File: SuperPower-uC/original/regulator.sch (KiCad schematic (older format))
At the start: 41 parts, among them Q701 DMP3028LSD, Q702 DMN3018SSD, Q703 2N7002A, U701 TPS63070RNMT, U702 TPS63070RNMT, U703 TPS70933DRVT

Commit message: Exchanged inductor of the regulators with IHLP2525CZER1R5M01
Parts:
- L701, L702: footprint Inductor_SMD:L_0603_1608Metric -> Inductor_SMD:L_Vishay_IHLP-2525; Ind_value (none) -> 1.5µH; Mfr_name (none) -> Vishay; Mfr_no (none) -> IHLP2525CZER1R5M01
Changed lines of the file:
@@
 F 0 "L701" V 6300 1750 50  0000 C CNN
 F 1 "1.5μH" V 6200 1750 50  0000 C CNN
-F 2 "Inductor_SMD:L_0603_1608Metric" H 6150 1750 50  0001 C CNN
-F 3 "https://datasheet.lcsc.com/szlcsc/TDK-MLZ1608A2R2WT000_C76797.pdf" H 6150 1750 50  0001 C CNN
+F 2 "Inductor_SMD:L_Vishay_IHLP-2525" H 6150 1750 50  0001 C CNN
+F 3 "https://www.mouser.de/datasheet/2/427/ihlp_2525cz_01-1763244.pdf" H 6150 1750 50  0001 C CNN
+F 4 "1.5µH" H 6150 1750 50  0001 C CNN "Ind_value"
+F 5 "Vishay" H 6150 1750 50  0001 C CNN "Mfr_name"
+F 6 "IHLP2525CZER1R5M01" H 6150 1750 50  0001 C CNN "Mfr_no"
 	1    6150 1750
 	0    -1   -1   0
@@
 F 0 "L702" V 6450 4800 50  0000 C CNN
 F 1 "1.5μH" V 6350 4800 50  0000 C CNN
-F 2 "Inductor_SMD:L_0603_1608Metric" H 6300 4800 50  0001 C CNN
-F 3 "https://datasheet.lcsc.com/szlcsc/TDK-MLZ1608A2R2WT000_C76797.pdf" H 6300 4800 50  0001 C CNN
+F 2 "Inductor_SMD:L_Vishay_IHLP-2525" H 6300 4800 50  0001 C CNN
+F 3 "https://www.mouser.de/datasheet/2/427/ihlp_2525cz_01-1763244.pdf" H 6300 4800 50  0001 C CNN
+F 4 "1.5µH" H 6300 4800 50  0001 C CNN "Ind_value"
+F 5 "Vishay" H 6300 4800 50  0001 C CNN "Mfr_name"
+F 6 "IHLP2525CZER1R5M01" H 6300 4800 50  0001 C CNN "Mfr_no"
 	1    6300 4800
 	0    -1   -1   0

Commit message: Changed regulator for 5V back to high side switching
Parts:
- removed R713: 100k, Resistor_SMD:R_0603_1608Metric, symbol Device:R_Small
- added JP3: Jumper_NC_Small, Connector_PinHeader_2.54mm:PinHeader_1x02_P2.54mm_Vertical, symbol Device:Jumper_NC_Small
- added Q9: 2N7002A, Package_TO_SOT_SMD:SOT-23, symbol 2n7002a:2N7002A
- added R18, R30: 1M, Resistor_SMD:R_0603_1608Metric, symbol Device:R_Small
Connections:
- net labels removed: GND_SW
- wire segments 184 -> 199
- no-connect marks 3 -> 1
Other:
- note added: "bypass\nEN_5V\n"
- moved on the sheet: C711, C712, C713, Q702A

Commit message: Update Buck-Boost inductors
Replace Vishay HILP series by TDK SPM series
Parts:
- removed L701, L702: 1.5μH, Inductor_SMD:L_Vishay_IHLP-2525, symbol Device:L
- added L701, L702: SPM6530T-1R5M, SPM6530T-1R5M:L_TDK_SPM6530T, symbol spm6530t-1r5m:SPM6530T-1R5M
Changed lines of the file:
@@
-$EndComp
-$Comp
-L Device:L L701
-U 1 1 5FBFC1E5
-P 6150 1750
-F 0 "L701" V 6300 1750 50  0000 C CNN
-F 1 "1.5μH" V 6200 1750 50  0000 C CNN
-F 2 "Inductor_SMD:L_Vishay_IHLP-2525" H 6150 1750 50  0001 C CNN
-F 3 "https://www.mouser.de/datasheet/2/427/ihlp_2525cz_01-1763244.pdf" H 6150 1750 50  0001 C CNN
-F 4 "1.5µH" H 6150 1750 50  0001 C CNN "Ind_value"
-F 5 "Vishay" H 6150 1750 50  0001 C CNN "Mfr_name"
-F 6 "IHLP2525CZER1R5M01" H 6150 1750 50  0001 C CNN "Mfr_no"
-	1    6150 1750
-	0    -1   -1   0
 $EndComp
 $Comp
@@
 	1    5400 5350
 	1    0    0    -1
-$EndComp
-$Comp
-L Device:L L702
-U 1 1 602F526D
-P 6300 4800
-F 0 "L702" V 6450 4800 50  0000 C CNN
-F 1 "1.5μH" V 6350 4800 50  0000 C CNN
-F 2 "Inductor_SMD:L_Vishay_IHLP-2525" H 6300 4800 50  0001 C CNN
-F 3 "https://www.mouser.de/datasheet/2/427/ihlp_2525cz_01-1763244.pdf" H 6300 4800 50  0001 C CNN
-F 4 "1.5µH" H 6300 4800 50  0001 C CNN "Ind_value"
-F 5 "Vishay" H 6300 4800 50  0001 C CNN "Mfr_name"
-F 6 "IHLP2525CZER1R5M01" H 6300 4800 50  0001 C CNN "Mfr_no"
-	1    6300 4800
-	0    -1   -1   0
 $EndComp
 Wire Wire Line
@@
 	8150 5850 8150 5600
 Connection ~ 8150 5600
+$Comp
+L spm6530t-1r5m:SPM6530T-1R5M L701
+U 1 1 5FDC75EF
+P 6150 1750
+F 0 "L701" V 6250 1850 50  0000 R CNN
+F 1 "SPM6530T-1R5M" V 6100 1900 50  0001 R CNN
+F 2 "SPM6530T-1R5M:L_TDK_SPM6530T" H 6150 1750 50  0001 C CNN
+F 3 "https://product.tdk.com/info/en/catalog/datasheets/inductor_commercial_power_spm6530_en.pdf" H 6150 1750 50  0001 C CNN
+F 4 "TDK" H 6150 1750 50  0001 C CNN "Mfr_name"
+F 5 "SPM6530T-1R5M100" H 6150 1750 50  0001 C CNN "Mfr_no"
+F 6 "6,5x7,1x3,0mm" H 6150 1750 50  0001 C CNN "Package"
+F 7 "1.5µH" V 6100 1850 50  0000 R CNN "Ind_value"
+F 8 "11.0A" H 6150 1750 50  0001 C CNN "Ind_current_max"
+F 9 "11.5A" H 6150 1750 50  0001 C CNN "Ind_current_sat_max"
+F 10 "9.70mOhm" V 6100 1850 50  0001 R CNN "Ind_DCR_typ"
+F 11 "20%" H 6150 1750 50  0001 C CNN "Ind_tol"
+F 12 ">10MHz" H 6150 1750 50  0001 C CNN "Ind_SFR"
+F 13 "https://octopart.com/spm6530t-1r5m100-tdk-9518783?r=sp" H 6150 1750 50  0001 C CNN "Octopart_link"
+F 14 "https://fr.farnell.com/tdk/spm6530t-1r5m100/inductance-1-5uh-20-blindee/dp/2215610?st=SPM6530T-1R5M100" H 6150 1750 50  0001 C CNN "Farnell_link"
+F 15 "2215610" H 6150 1750 50  0001 C CNN "Farnell_ref"
+F 16 "2020-12-16" H 6150 1750 50  0001 C CNN "Farnell_check_date"
+F 17 "1,36 €" H 6150 1750 50  0001 C CNN "Farnell_price_qt=1"
+F 18 "1,36 €" H 6150 1750 50  0001 C CNN "Farnell_price_qt=10"
+F 19 "0,738 €" H 6150 1750 50  0001 C CNN "Farnell_price_qt=100"
+F 20 "0,458 €" H 6150 1750 50  0001 C CNN "Farnell_price_qt=1000"
+F 21 "2" H 6150 1750 50  0001 C CNN "Farnell_stock"
+F 22 "https://lcsc.com/product-detail/Power-Inductors_TDK-SPM6530T-1R5M100_C76854.html" H 6150 1750 50  0001 C CNN "LCSC_link"
+F 23 "C76854" H 6150 1750 50  0001 C CNN "LCSC_ref"
+F 24 "2020-12-16" H 6150 1750 50  0001 C CNN "LCSC_check_date"
+F 25 "$0.1717" H 6150 1750 50  0001 C CNN "LCSC_price_qt=1"
+F 26 "$0.1324" H 6150 1750 50  0001 C CNN "LCSC_price_qt=10"
+F 27 "$0.1179" H 6150 1750 50  0001 C CNN "LCSC_price_qt=100"
+F 28 "$0.1131" H 6150 1750 50  0001 C CNN "LCSC_price_qt=1000"
+F 29 "10,496" H 6150 1750 50  0001 C CNN "LCSC_stock"
+F 30 "https://eu.mouser.com/ProductDetail/TDK/SPM6530T-1R5M100/?qs=chjFIDm9dbqQ8Uh0Ilzv2g%3D%3D" H 6150 1750 50  0001 C CNN "Mouser_link"
+F 31 "810-SPM6530T-1R5M100" H 6150 1750 50  0001 C CNN "Mouser_ref"
+F 32 "2020-12-16" H 6150 1750 50  0001 C CNN "Mouser_check_date"
+F 33 "$1.42" H 6150 1750 50  0001 C CNN "Mouser_price_qt=1"
+F 34 "$1.07" H 6150 1750 50  0001 C CNN "Mouser_price_qt=10"
+F 35 "$0.812" H 6150 1750 50  0001 C CNN "Mouser_price_qt=100"
+F 36 "$0.564" H 6150 1750 50  0001 C CNN "Mouser_price_qt=1000"
+F 37 "2,011" H 6150 1750 50  0001 C CNN "Mouser_stock"
+F 38 "-" H 6150 1750 50  0001 C CNN "RS_link"
+F 39 "-" H 6150 1750 50  0001 C CNN "RS_ref"
+F 40 "2020-12-16" H 6150 1750 50  0001 C CNN "RS_check_date"
+F 41 "-" H 6150 1750 50  0001 C CNN "RS_price_qt=1"
+F 42 "-" H 6150 1750 50  0001 C CNN "RS_price_qt=10"
+F 43 "-" H 6150 1750 50  0001 C CNN "RS_price_qt=100"
+F 44 "-" H 6150 1750 50  0001 C CNN "RS_price_qt=1000"
+F 45 "-" H 6150 1750 50  0001 C CNN "RS_stock"
+F 46 "TO_CHECK" H 6150 1750 50  0001 C CNN "Status"
+F 47 "1.00" H 6150 1750 50  0001 C CNN "Release_version"
+F 48 "2020-12-16" H 6150 1750 50  0001 C CNN "Release_date"
+F 49 "ManWithNoName" H 6150 1750 50  0001 C CNN "Designer"
+	1    6150 1750
+	0    -1   -1   0
+$EndComp
+$Comp
+L spm6530t-1r5m:SPM6530T-1R5M L702
+U 1 1 5FE1ED88
+P 6300 4800
+F 0 "L702" V 6400 4900 50  0000 R CNN
+F 1 "SPM6530T-1R5M" V 6250 4950 50  0001 R CNN
+F 2 "SPM6530T-1R5M:L_TDK_SPM6530T" H 6300 4800 50  0001 C CNN
+F 3 "https://product.tdk.com/info/en/catalog/datasheets/inductor_commercial_power_spm6530_en.pdf" H 6300 4800 50  0001 C CNN
+F 4 "TDK" H 6300 4800 50  0001 C CNN "Mfr_name"
+F 5 "SPM6530T-1R5M100" H 6300 4800 50  0001 C CNN "Mfr_no"
+F 6 "6,5x7,1x3,0mm" H 6300 4800 50  0001 C CNN "Package"
+F 7 "1.5µH" V 6250 4900 50  0000 R CNN "Ind_value"
+F 8 "11.0A" H 6300 4800 50  0001 C CNN "Ind_current_max"
+F 9 "11.5A" H 6300 4800 50  0001 C CNN "Ind_current_sat_max"
+F 10 "9.70mOhm" V 6250 4900 50  0001 R CNN "Ind_DCR_typ"
+F 11 "20%" H 6300 4800 50  0001 C CNN "Ind_tol"
+F 12 ">10MHz" H 6300 4800 50  0001 C CNN "Ind_SFR"
+F 13 "https://octopart.com/spm6530t-1r5m100-tdk-9518783?r=sp" H 6300 4800 50  0001 C CNN "Octopart_link"
+F 14 "https://fr.farnell.com/tdk/spm6530t-1r5m100/inductance-1-5uh-20-blindee/dp/2215610?st=SPM6530T-1R5M100" H 6300 4800 50  0001 C CNN "Farnell_link"
+F 15 "2215610" H 6300 4800 50  0001 C CNN "Farnell_ref"
+F 16 "2020-12-16" H 6300 4800 50  0001 C CNN "Farnell_check_date"
+F 17 "1,36 €" H 6300 4800 50  0001 C CNN "Farnell_price_qt=1"
+F 18 "1,36 €" H 6300 4800 50  0001 C CNN "Farnell_price_qt=10"
+F 19 "0,738 €" H 6300 4800 50  0001 C CNN "Farnell_price_qt=100"
+F 20 "0,458 €" H 6300 4800 50  0001 C CNN "Farnell_price_qt=1000"
+F 21 "2" H 6300 4800 50  0001 C CNN "Farnell_stock"
+F 22 "https://lcsc.com/product-detail/Power-Inductors_TDK-SPM6530T-1R5M100_C76854.html" H 6300 4800 50  0001 C CNN "LCSC_link"
+F 23 "C76854" H 6300 4800 50  0001 C CNN "LCSC_ref"
+F 24 "2020-12-16" H 6300 4800 50  0001 C CNN "LCSC_check_date"
+F 25 "$0.1717" H 6300 4800 50  0001 C CNN "LCSC_price_qt=1"
+F 26 "$0.1324" H 6300 4800 50  0001 C CNN "LCSC_price_qt=10"
+F 27 "$0.1179" H 6300 4800 50  0001 C CNN "LCSC_price_qt=100"
+F 28 "$0.1131" H 6300 4800 50  0001 C CNN "LCSC_price_qt=1000"
+F 29 "10,496" H 6300 4800 50  0001 C CNN "LCSC_stock"
+F 30 "https://eu.mouser.com/ProductDetail/TDK/SPM6530T-1R5M100/?qs=chjFIDm9dbqQ8Uh0Ilzv2g%3D%3D" H 6300 4800 50  0001 C CNN "Mouser_link"
+F 31 "810-SPM6530T-1R5M100" H 6300 4800 50  0001 C CNN "Mouser_ref"
+F 32 "2020-12-16" H 6300 4800 50  0001 C CNN "Mouser_check_date"
+F 33 "$1.42" H 6300 4800 50  0001 C CNN "Mouser_price_qt=1"
+F 34 "$1.07" H 6300 4800 50  0001 C CNN "Mouser_price_qt=10"
+F 35 "$0.812" H 6300 4800 50  0001 C CNN "Mouser_price_qt=100"
+F 36 "$0.564" H 6300 4800 50  0001 C CNN "Mouser_price_qt=1000"
+F 37 "2,011" H 6300 4800 50  0001 C CNN "Mouser_stock"
+F 38 "-" H 6300 4800 50  0001 C CNN "RS_link"
+F 39 "-" H 6300 4800 50  0001 C CNN "RS_ref"
+F 40 "2020-12-16" H 6300 4800 50  0001 C CNN "RS_check_date"
+F 41 "-" H 6300 4800 50  0001 C CNN "RS_price_qt=1"
+F 42 "-" H 6300 4800 50  0001 C CNN "RS_price_qt=10"
+F 43 "-" H 6300 4800 50  0001 C CNN "RS_price_qt=100"
+F 44 "-" H 6300 4800 50  0001 C CNN "RS_price_qt=1000"
+F 45 "-" H 6300 4800 50  0001 C CNN "RS_stock"
+F 46 "TO_CHECK" H 6300 4800 50  0001 C CNN "Status"
+F 47 "1.00" H 6300 4800 50  0001 C CNN "Release_version"
+F 48 "2020-12-16" H 6300 4800 50  0001 C CNN "Release_date"
+F 49 "ManWithNoName" H 6300 4800 50  0001 C CNN "Designer"
+	1    6300 4800
+	0    -1   -1   0
+$EndComp
 $EndSCHEMATC

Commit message: Re-Annotate project
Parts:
- renumbered C710 to C14, C709 to C15, C701 to C16, C702 to C17, C711 to C18, C703 to C19, C712 to C20, C713 to C21, C707 to C22, C717 to C23, C708 to C24, C718 to C25, C704 to C26, C714 to C27, C705 to C28, C715 to C29, C706 to C30, C716 to C31, L701 to L2, L702 to L3, Q703 to Q10, Q9 to Q11, Q701 to Q5, Q702 to Q9, R711 to R39, R17 to R40, R18 to R41, R16 to R42, R30 to R43, R705 to R44, R709 to R45, R704 to R46, R703 to R47, R708 to R48, R707 to R49, R701 to R50, R706 to R51, TP37 to TP32, TP41 to TP33, U702 to U10, U703 to U8, U701 to U9
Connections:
- net EN_3V3: now also Q9.2 (G); no longer Q9.4 (G)
- net GND: now also Q9.1 (S); no longer Q9.3 (S)
- net GND_3v3: now also Q9.7 (D), Q9.8 (D); no longer Q9.5 (D), Q9.6 (D)
- net VIN: now also Q9.5 (D), Q9.6 (D); no longer Q9.7 (D), Q9.8 (D)
- net at JP3.1, Q11.3 (D), R43.1: now also Q9.4 (G); no longer Q9.2 (G)
- net at C18.1, C20.1, C21.1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: now also Q9.3 (S); no longer Q9.1 (S)

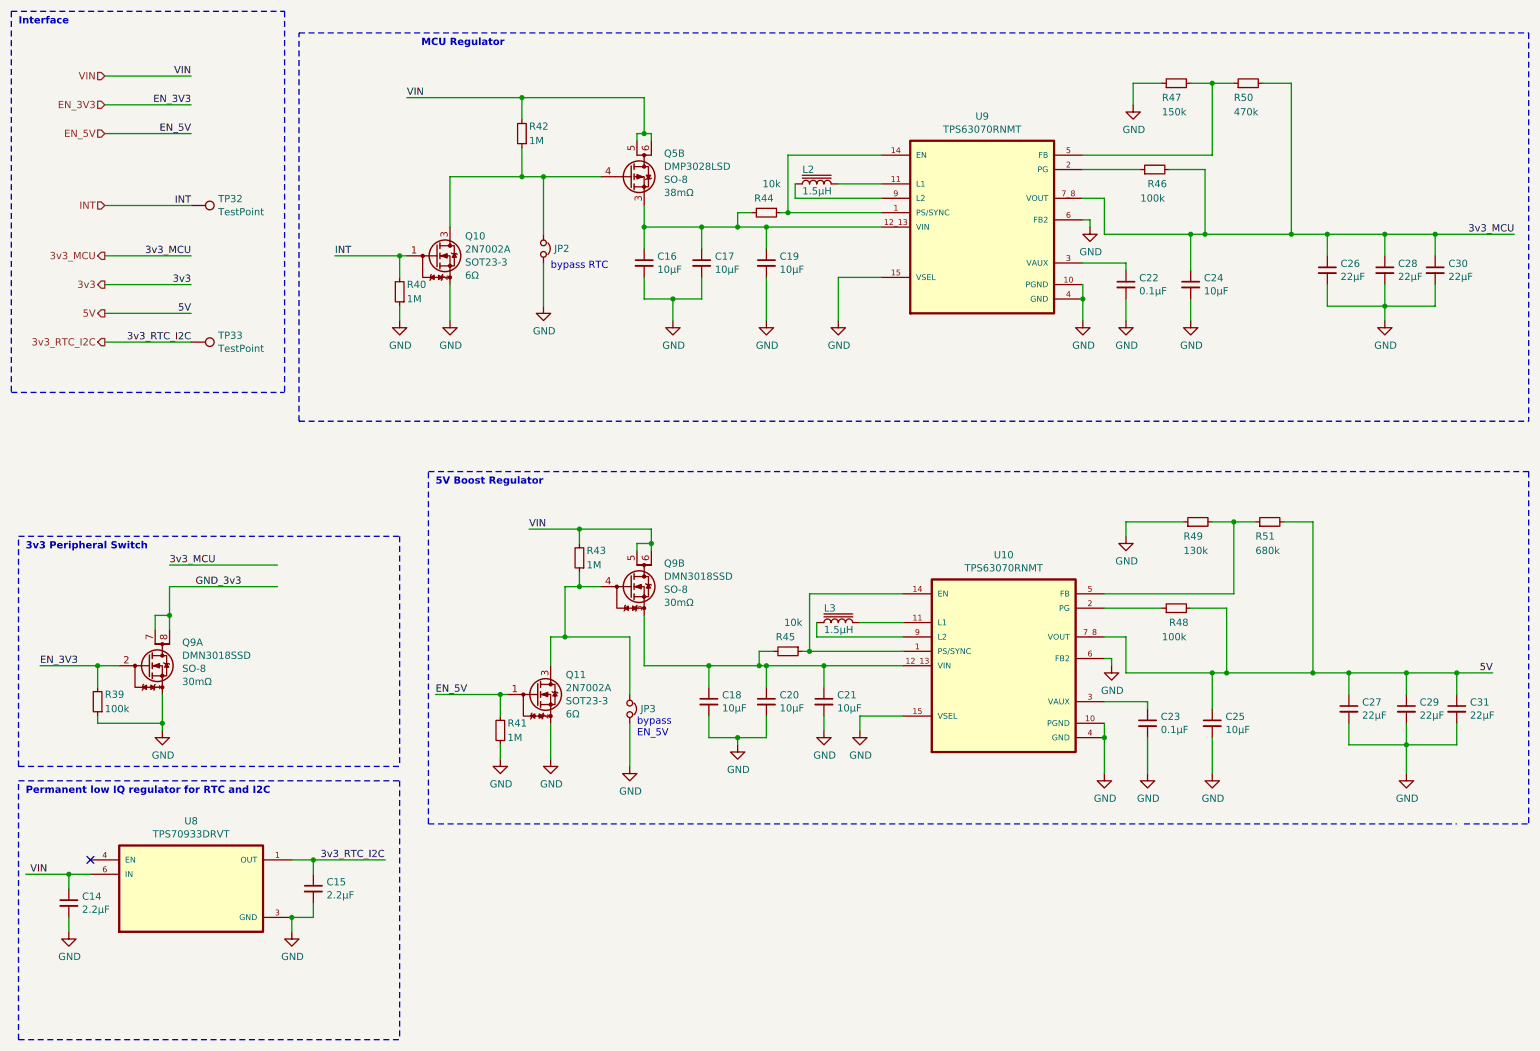
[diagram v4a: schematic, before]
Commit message: Replace some dual P-MOSFETs by SOT23-6 P-MOSFETs
+ resolve some issues (2 P-MOSFETs at Buck-Boost stage were reversed)
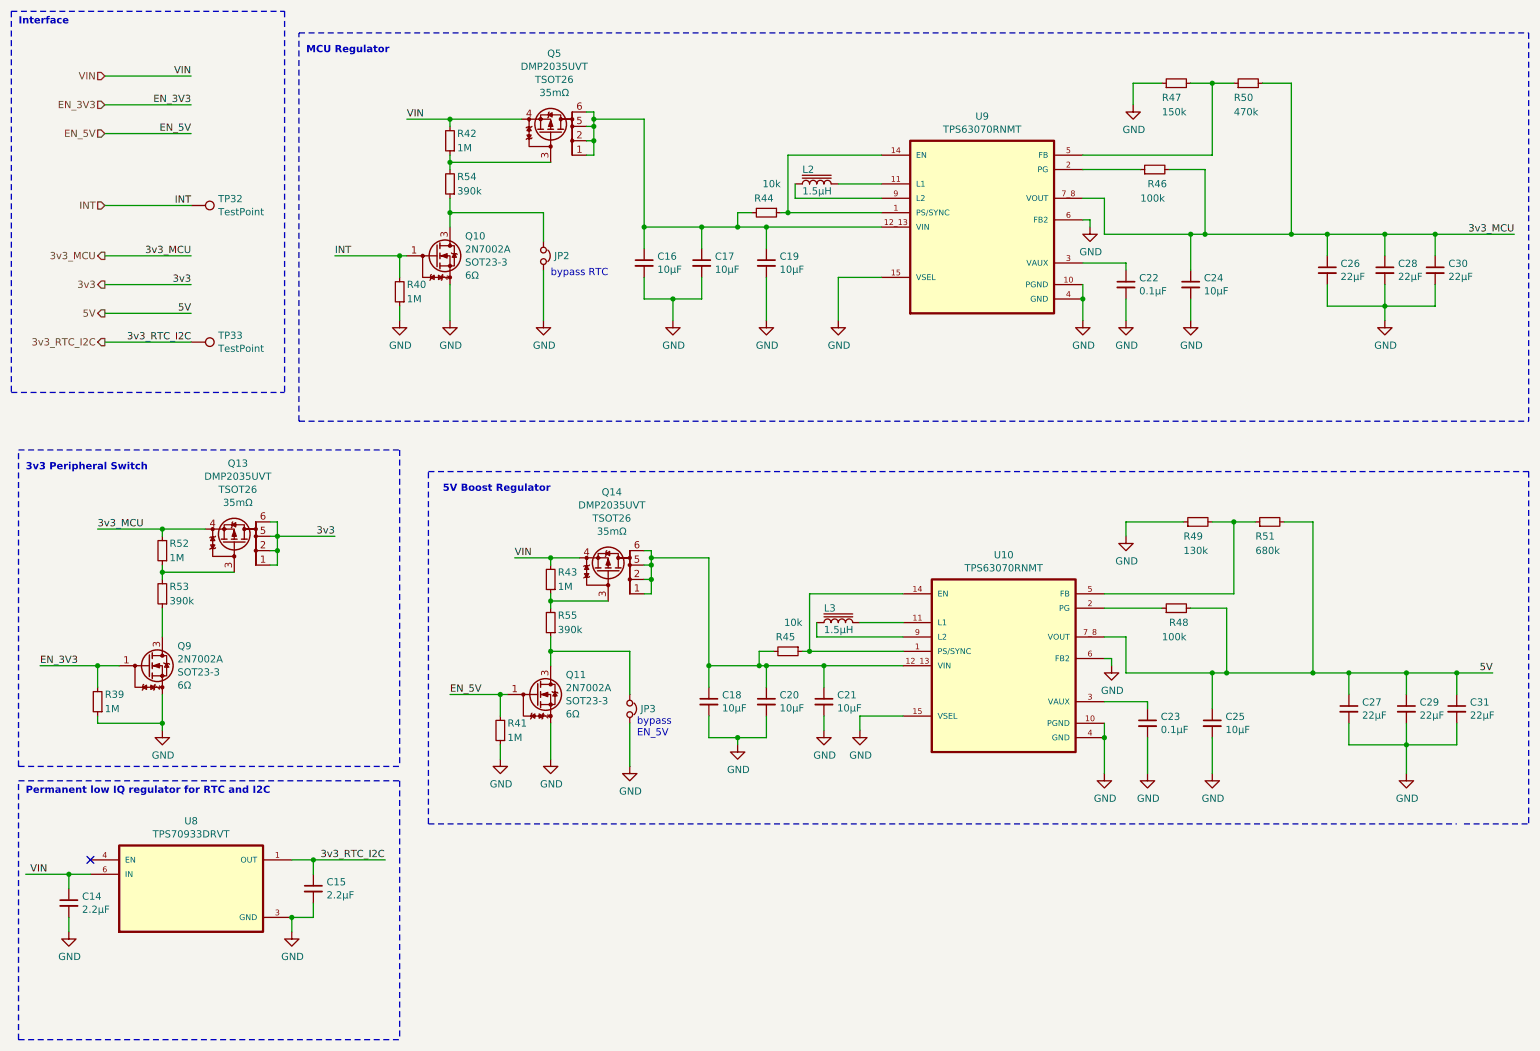
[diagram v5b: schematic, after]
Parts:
- removed Q5: DMP3028LSD, Package_SO:SO-8_3.9x4.9mm_P1.27mm, symbol dmp3028lsd:DMP3028LSD
- removed Q9: DMN3018SSD, Package_SO:SO-8_3.9x4.9mm_P1.27mm, symbol dmn3018ssd:DMN3018SSD
- added Q13, Q14, Q5: DMP2035UVT, Package_TO_SOT_SMD:SOT-23-6, symbol dmp2035uvt:DMP2035UVT
- added Q9: 2N7002A, Package_TO_SOT_SMD:SOT-23, symbol 2n7002a:2N7002A
- added R52: 1M, Resistor_SMD:R_0603_1608Metric, symbol Device:R_Small
- added R53, R54, R55: 390k, Resistor_SMD:R_0603_1608Metric, symbol Device:R_Small
- R39: value 100k -> 1M
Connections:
- net 3v3: now also Q13.1 (D), Q13.2 (D), Q13.5 (D), Q13.6 (D)
- net 3v3_MCU: now also Q13.4 (S), R52.2
- net EN_3V3: now also Q9.1 (G)
- net GND: now also Q9.2 (S)
- net VIN: now also Q14.4 (S), Q5.4 (S)
- net at C16.1, C17.1, C19.1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: now also Q5.1 (D), Q5.2 (D), Q5.5 (D), Q5.6 (D)
- net at JP2.1, Q10.3 (D): now also R54.1; no longer R42.1
- net at JP3.1, Q11.3 (D): now also R55.1; no longer R43.1
- net at C18.1, C20.1, C21.1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: now also Q14.1 (D), Q14.2 (D), Q14.5 (D), Q14.6 (D)
- new net: Q5.3 (G), R42.1, R54.2
- new net: Q14.3 (G), R43.1, R55.2
- new net: Q13.3 (G), R52.1, R53.2
- new net: Q9.3 (D), R53.1
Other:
- moved on the sheet: JP2, R42, R43

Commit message: Add 3D file to every component
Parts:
- JP2, JP3: footprint Connector_PinHeader_2.54mm:PinHeader_1x02_P2.54mm_Vertical -> Jumper:SolderJumper-2_P1.3mm_Open_TrianglePad1.0x1.5mm
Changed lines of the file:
@@
 AR Path="/5FB04DFE" Ref="U?"  Part="1"
 AR Path="/5F63A0E9/5FB04DFE" Ref="U9"  Part="1"
+AR Path="/5F63B107/5FB04DFE" Ref="U9"  Part="1"
 F 0 "U9" H 7300 2820 50  0000 C CNN
 F 1 "TPS63070RNMT" H 7300 2729 50  0000 C CNN
@@
 F 0 "JP2" V 4250 2325 50  0000 L CNN
 F 1 "Jumper_NC_Small" V 4295 2324 50  0001 L CNN
-F 2 "Connector_PinHeader_2.54mm:PinHeader_1x02_P2.54mm_Vertical" H 4250 2250 50  0001 C CNN
+F 2 "Jumper:SolderJumper-2_P1.3mm_Open_TrianglePad1.0x1.5mm" H 4250 2250 50  0001 C CNN
 F 3 "~" H 4250 2250 50  0001 C CNN
 	1    4250 2250
@@
 F 0 "JP3" V 4850 5475 50  0000 L CNN
 F 1 "Jumper_NC_Small" V 4895 5474 50  0001 L CNN
-F 2 "Connector_PinHeader_2.54mm:PinHeader_1x02_P2.54mm_Vertical" H 4850 5400 50  0001 C CNN
+F 2 "Jumper:SolderJumper-2_P1.3mm_Open_TrianglePad1.0x1.5mm" H 4850 5400 50  0001 C CNN
 F 3 "~" H 4850 5400 50  0001 C CNN
 	1    4850 5400

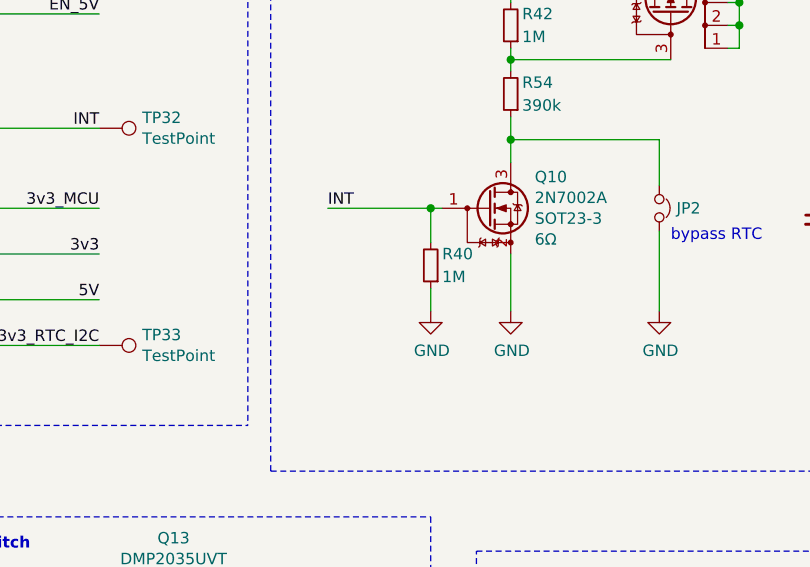
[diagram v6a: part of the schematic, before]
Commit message: Remove R40 + Update Terminal Block Footprint
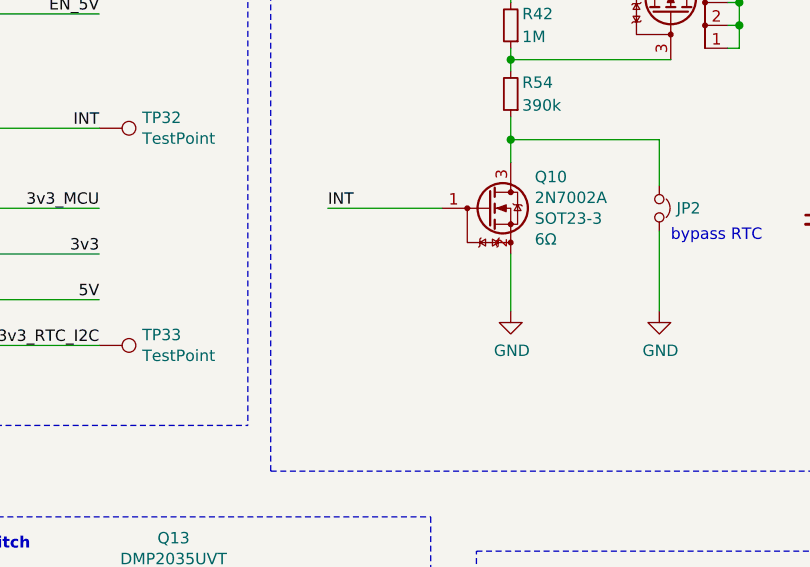
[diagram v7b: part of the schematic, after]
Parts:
- removed R40: 1M, Resistor_SMD:R_0603_1608Metric, symbol Device:R_Small
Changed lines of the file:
@@
 	3600 1550 3600 1600
-Wire Wire Line
-	3300 2250 3250 2250
-Connection ~ 3250 2250
 Wire Wire Line
 	8300 4100 8700 4100
@@
 Wire Wire Line
 	3600 2700 3600 2450
-$Comp
-L Device:R_Small R40
-U 1 1 5FC79983
-P 3250 2500
-F 0 "R40" H 3200 2450 50  0000 R CNN
-F 1 "1M" H 3200 2550 50  0000 R CNN
-F 2 "Resistor_SMD:R_0603_1608Metric" H 3250 2500 50  0001 C CNN
-F 3 "~" H 3250 2500 50  0001 C CNN
-	1    3250 2500
-	-1   0    0    1
-$EndComp
-Wire Wire Line
-	3250 2250 3250 2400
-$Comp
-L power:GND #PWR059
-U 1 1 5FC83D8B
-P 3250 2700
-F 0 "#PWR059" H 3250 2450 50  0001 C CNN
-F 1 "GND" H 3255 2527 50  0000 C CNN
-F 2 "" H 3250 2700 50  0001 C CNN
-F 3 "" H 3250 2700 50  0001 C CNN
-	1    3250 2700
-	1    0    0    -1
-$EndComp
-Wire Wire Line
-	3250 2600 3250 2700
 Wire Wire Line
 	1600 5300 1600 5500
@@
 Wire Notes Line
 	550  550  2450 550
-Wire Wire Line
-	2800 2250 3250 2250
 $Comp
 L 2n7002a:2N7002A Q10
@@
 Wire Wire Line
 	4600 1300 4600 1350
+Wire Wire Line
+	2800 2250 3300 2250
 $EndSCHEMATC
